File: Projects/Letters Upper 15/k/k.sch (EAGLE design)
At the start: 42 parts

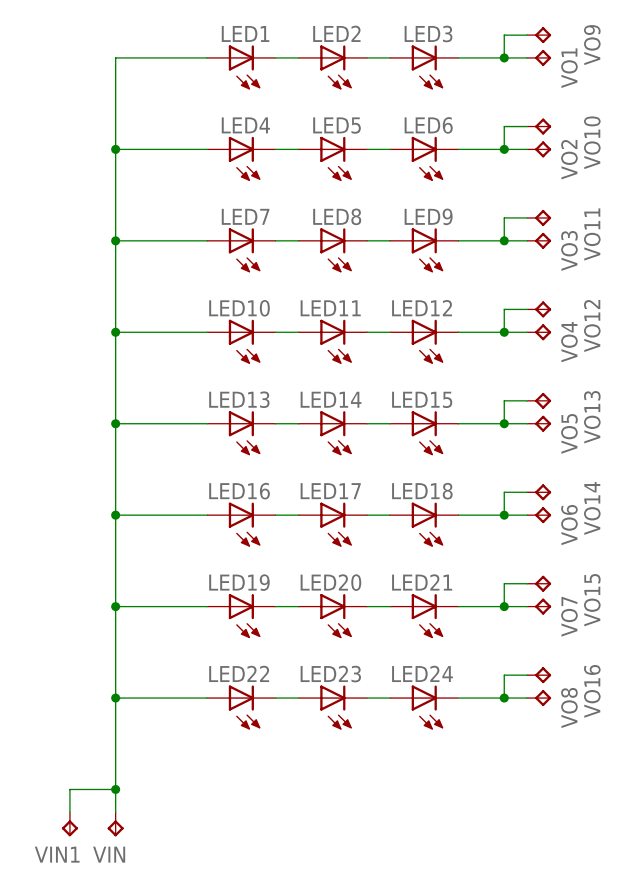
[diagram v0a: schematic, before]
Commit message: 
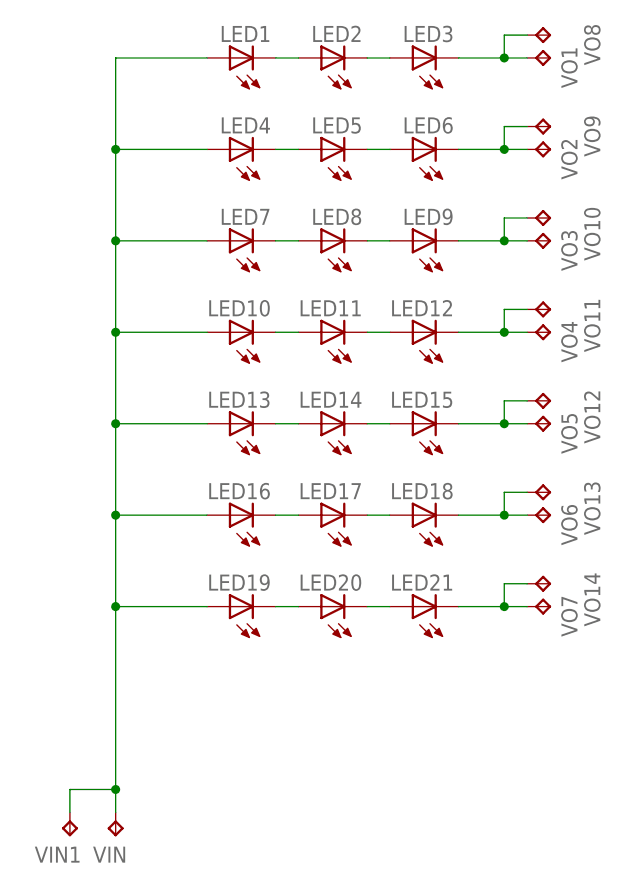
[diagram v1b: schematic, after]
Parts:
- removed LED22, LED23, LED24: (no value), CyberRailGuru:LED0805
- removed VO15, VO16: (no value), CyberRailGuru:TEST_POINTPAD1-20
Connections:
- removed net N$1: LED22.C, LED23.A
- removed net N$2: LED23.C, LED24.A
- removed net N$5: LED24.C, VO16.TP, VO8.TP
- net VIN: no longer LED22.A
- net VOUT1: now also VO8.TP; no longer VO9.TP
- net VOUT2: now also VO9.TP; no longer VO10.TP
- net VOUT3: now also VO10.TP; no longer VO11.TP
- net VOUT4: now also VO11.TP; no longer VO12.TP
- net VOUT5: now also VO12.TP; no longer VO13.TP
- net VOUT6: now also VO13.TP; no longer VO14.TP
- net VOUT7: now also VO14.TP; no longer VO15.TP
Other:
- moved on the sheet: VO10, VO11, VO12, VO13, VO14, VO8, VO9
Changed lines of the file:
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@@
 <part name="VO7" library="CyberRailGuru" deviceset="TEST_POINT" device="PAD1-20"/>
 <part name="VIN1" library="CyberRailGuru" deviceset="TEST_POINT" device="PAD1-20"/>
+<part name="VO8" library="CyberRailGuru" deviceset="TEST_POINT" device="PAD1-20"/>
 <part name="VO9" library="CyberRailGuru" deviceset="TEST_POINT" device="PAD1-20"/>
 <part name="VO10" library="CyberRailGuru" deviceset="TEST_POINT" device="PAD1-20"/>
@@
 <part name="VO13" library="CyberRailGuru" deviceset="TEST_POINT" device="PAD1-20"/>
 <part name="VO14" library="CyberRailGuru" deviceset="TEST_POINT" device="PAD1-20"/>
-<part name="VO15" library="CyberRailGuru" deviceset="TEST_POINT" device="PAD1-20"/>
-<part name="LED22" library="CyberRailGuru" deviceset="LED" device="0805"/>
-<part name="LED23" library="CyberRailGuru" deviceset="LED" device="0805"/>
-<part name="LED24" library="CyberRailGuru" deviceset="LED" device="0805"/>
-<part name="VO8" library="CyberRailGuru" deviceset="TEST_POINT" device="PAD1-20"/>
-<part name="VO16" library="CyberRailGuru" deviceset="TEST_POINT" device="PAD1-20"/>
 </parts>
 <sheets>
@@
 </instance>
 <instance part="VIN1" gate="G$1" x="40.64" y="152.4" rot="R180"/>
-<instance part="VO9" gate="G$1" x="93.98" y="241.3" smashed="yes" rot="R270">
+<instance part="VO8" gate="G$1" x="93.98" y="241.3" smashed="yes" rot="R270">
 <attribute name="NAME" x="97.79" y="242.57" size="1.778" layer="95" rot="R270"/>
 <attribute name="VALUE" x="92.71" y="240.03" size="1.778" layer="96" rot="R270"/>
 </instance>
-<instance part="VO10" gate="G$1" x="93.98" y="231.14" smashed="yes" rot="R270">
+<instance part="VO9" gate="G$1" x="93.98" y="231.14" smashed="yes" rot="R270">
 <attribute name="NAME" x="97.79" y="232.41" size="1.778" layer="95" rot="R270"/>
 <attribute name="VALUE" x="92.71" y="229.87" size="1.778" layer="96" rot="R270"/>
 </instance>
-<instance part="VO11" gate="G$1" x="93.98" y="220.98" smashed="yes" rot="R270">
+<instance part="VO10" gate="G$1" x="93.98" y="220.98" smashed="yes" rot="R270">
 <attribute name="NAME" x="97.79" y="222.25" size="1.778" layer="95" rot="R270"/>
 <attribute name="VALUE" x="92.71" y="219.71" size="1.778" layer="96" rot="R270"/>
 </instance>
-<instance part="VO12" gate="G$1" x="93.98" y="210.82" smashed="yes" rot="R270">
+<instance part="VO11" gate="G$1" x="93.98" y="210.82" smashed="yes" rot="R270">
 <attribute name="NAME" x="97.79" y="212.09" size="1.778" layer="95" rot="R270"/>
 <attribute name="VALUE" x="92.71" y="209.55" size="1.778" layer="96" rot="R270"/>
 </instance>
-<instance part="VO13" gate="G$1" x="93.98" y="200.66" smashed="yes" rot="R270">
+<instance part="VO12" gate="G$1" x="93.98" y="200.66" smashed="yes" rot="R270">
 <attribute name="NAME" x="97.79" y="201.93" size="1.778" layer="95" rot="R270"/>
 <attribute name="VALUE" x="92.71" y="199.39" size="1.778" layer="96" rot="R270"/>
 </instance>
-<instance part="VO14" gate="G$1" x="93.98" y="190.5" smashed="yes" rot="R270">
+<instance part="VO13" gate="G$1" x="93.98" y="190.5" smashed="yes" rot="R270">
 <attribute name="NAME" x="97.79" y="191.77" size="1.778" layer="95" rot="R270"/>
 <attribute name="VALUE" x="92.71" y="189.23" size="1.778" layer="96" rot="R270"/>
 </instance>
-<instance part="VO15" gate="G$1" x="93.98" y="180.34" smashed="yes" rot="R270">
+<instance part="VO14" gate="G$1" x="93.98" y="180.34" smashed="yes" rot="R270">
 <attribute name="NAME" x="97.79" y="181.61" size="1.778" layer="95" rot="R270"/>
 <attribute name="VALUE" x="92.71" y="179.07" size="1.778" layer="96" rot="R270"/>
-</instance>
-<instance part="LED22" gate="G$1" x="58.42" y="167.64" rot="R90"/>
-<instance part="LED23" gate="G$1" x="68.58" y="167.64" rot="R90"/>
-<instance part="LED24" gate="G$1" x="78.74" y="167.64" rot="R90"/>
-<instance part="VO8" gate="G$1" x="93.98" y="167.64" smashed="yes" rot="R270">
-<attribute name="NAME" x="95.25" y="168.91" size="1.778" layer="95" rot="R270"/>
-<attribute name="VALUE" x="92.71" y="166.37" size="1.778" layer="96" rot="R270"/>
-</instance>
-<instance part="VO16" gate="G$1" x="93.98" y="170.18" smashed="yes" rot="R270">
-<attribute name="NAME" x="97.79" y="171.45" size="1.778" layer="95" rot="R270"/>
-<attribute name="VALUE" x="92.71" y="168.91" size="1.778" layer="96" rot="R270"/>
 </instance>
 </instances>
@@
 <wire x1="83.82" y1="238.76" x2="88.9" y2="238.76" width="0.1524" layer="91"/>
 <pinref part="VO1" gate="G$1" pin="TP"/>
-<pinref part="VO9" gate="G$1" pin="TP"/>
+<pinref part="VO8" gate="G$1" pin="TP"/>
 <wire x1="88.9" y1="238.76" x2="91.44" y2="238.76" width="0.1524" layer="91"/>
 <wire x1="91.44" y1="241.3" x2="88.9" y2="241.3" width="0.1524" layer="91"/>
@@
 <wire x1="83.82" y1="228.6" x2="88.9" y2="228.6" width="0.1524" layer="91"/>
 <pinref part="VO2" gate="G$1" pin="TP"/>
-<pinref part="VO10" gate="G$1" pin="TP"/>
+<pinref part="VO9" gate="G$1" pin="TP"/>
 <wire x1="88.9" y1="228.6" x2="91.44" y2="228.6" width="0.1524" layer="91"/>
 <wire x1="91.44" y1="231.14" x2="88.9" y2="231.14" width="0.1524" layer="91"/>
@@
 <wire x1="83.82" y1="218.44" x2="88.9" y2="218.44" width="0.1524" layer="91"/>
 <pinref part="VO3" gate="G$1" pin="TP"/>
-<pinref part="VO11" gate="G$1" pin="TP"/>
+<pinref part="VO10" gate="G$1" pin="TP"/>
 <wire x1="88.9" y1="218.44" x2="91.44" y2="218.44" width="0.1524" layer="91"/>
 <wire x1="91.44" y1="220.98" x2="88.9" y2="220.98" width="0.1524" layer="91"/>
@@
 <wire x1="83.82" y1="208.28" x2="88.9" y2="208.28" width="0.1524" layer="91"/>
 <pinref part="VO4" gate="G$1" pin="TP"/>
-<pinref part="VO12" gate="G$1" pin="TP"/>
+<pinref part="VO11" gate="G$1" pin="TP"/>
 <wire x1="88.9" y1="208.28" x2="91.44" y2="208.28" width="0.1524" layer="91"/>
 <wire x1="91.44" y1="210.82" x2="88.9" y2="210.82" width="0.1524" layer="91"/>
@@
 <wire x1="83.82" y1="198.12" x2="88.9" y2="198.12" width="0.1524" layer="91"/>
 <pinref part="VO5" gate="G$1" pin="TP"/>
-<pinref part="VO13" gate="G$1" pin="TP"/>
+<pinref part="VO12" gate="G$1" pin="TP"/>
 <wire x1="88.9" y1="198.12" x2="91.44" y2="198.12" width="0.1524" layer="91"/>
 <wire x1="91.44" y1="200.66" x2="88.9" y2="200.66" width="0.1524" layer="91"/>
@@
 <wire x1="83.82" y1="187.96" x2="88.9" y2="187.96" width="0.1524" layer="91"/>
 <pinref part="VO6" gate="G$1" pin="TP"/>
-<pinref part="VO14" gate="G$1" pin="TP"/>
+<pinref part="VO13" gate="G$1" pin="TP"/>
 <wire x1="88.9" y1="187.96" x2="91.44" y2="187.96" width="0.1524" layer="91"/>
 <wire x1="91.44" y1="190.5" x2="88.9" y2="190.5" width="0.1524" layer="91"/>
@@
 <wire x1="83.82" y1="177.8" x2="88.9" y2="177.8" width="0.1524" layer="91"/>
 <pinref part="VO7" gate="G$1" pin="TP"/>
-<pinref part="VO15" gate="G$1" pin="TP"/>
+<pinref part="VO14" gate="G$1" pin="TP"/>
 <wire x1="88.9" y1="177.8" x2="91.44" y2="177.8" width="0.1524" layer="91"/>
 <wire x1="91.44" y1="180.34" x2="88.9" y2="180.34" width="0.1524" layer="91"/>
@@
 <wire x1="45.72" y1="198.12" x2="45.72" y2="187.96" width="0.1524" layer="91"/>
 <wire x1="45.72" y1="187.96" x2="45.72" y2="177.8" width="0.1524" layer="91"/>
-<wire x1="45.72" y1="177.8" x2="45.72" y2="167.64" width="0.1524" layer="91"/>
-<wire x1="45.72" y1="167.64" x2="45.72" y2="157.48" width="0.1524" layer="91"/>
+<wire x1="45.72" y1="177.8" x2="45.72" y2="157.48" width="0.1524" layer="91"/>
 <wire x1="45.72" y1="157.48" x2="45.72" y2="154.94" width="0.1524" layer="91"/>
 <wire x1="55.88" y1="177.8" x2="45.72" y2="177.8" width="0.1524" layer="91"/>
@@
 <wire x1="40.64" y1="157.48" x2="45.72" y2="157.48" width="0.1524" layer="91"/>
 <junction x="45.72" y="157.48"/>
-<pinref part="LED22" gate="G$1" pin="A"/>
-<wire x1="55.88" y1="167.64" x2="45.72" y2="167.64" width="0.1524" layer="91"/>
-<junction x="45.72" y="167.64"/>
-</segment>
-</net>
-<net name="N$1" class="0">
-<segment>
-<pinref part="LED23" gate="G$1" pin="A"/>
-<pinref part="LED22" gate="G$1" pin="C"/>
-<wire x1="66.04" y1="167.64" x2="63.5" y2="167.64" width="0.1524" layer="91"/>
-</segment>
-</net>
-<net name="N$2" class="0">
-<segment>
-<pinref part="LED24" gate="G$1" pin="A"/>
-<pinref part="LED23" gate="G$1" pin="C"/>
-<wire x1="76.2" y1="167.64" x2="73.66" y2="167.64" width="0.1524" layer="91"/>
-</segment>
-</net>
-<net name="N$5" class="0">
-<segment>
-<pinref part="VO8" gate="G$1" pin="TP"/>
-<pinref part="LED24" gate="G$1" pin="C"/>
-<wire x1="91.44" y1="167.64" x2="88.9" y2="167.64" width="0.1524" layer="91"/>
-<pinref part="VO16" gate="G$1" pin="TP"/>
-<wire x1="88.9" y1="167.64" x2="83.82" y2="167.64" width="0.1524" layer="91"/>
-<wire x1="91.44" y1="170.18" x2="88.9" y2="170.18" width="0.1524" layer="91"/>
-<wire x1="88.9" y1="170.18" x2="88.9" y2="167.64" width="0.1524" layer="91"/>
-<junction x="88.9" y="167.64"/>
-</segment>
-</net>
+</segment>
+</net>
